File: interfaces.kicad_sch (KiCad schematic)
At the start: 125 parts, among them J3 USB-Micro-B_Amphenol_10118192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, J6 PinHeader_2x7_P2mm_Drill0.9mm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, J7 PinHeader_1x6_P2.54mm_Drill1.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, U1 MTFC16GAPALNA-AIT, U14 XC7A100T-FGG484, U17 USB3300-EZK-TR, U18 USB3300-EZK-TR, U19 FT4232H_QFN, U21 LSF0108RKSR, U22 LSF0101DRYR, U23 Oscillator_24MHz_ASEMB, U24 Oscillator_24MHz_ASEMB, U6 NVT2008BQ,115, Y1 Resonator_12MHz_ABM8G

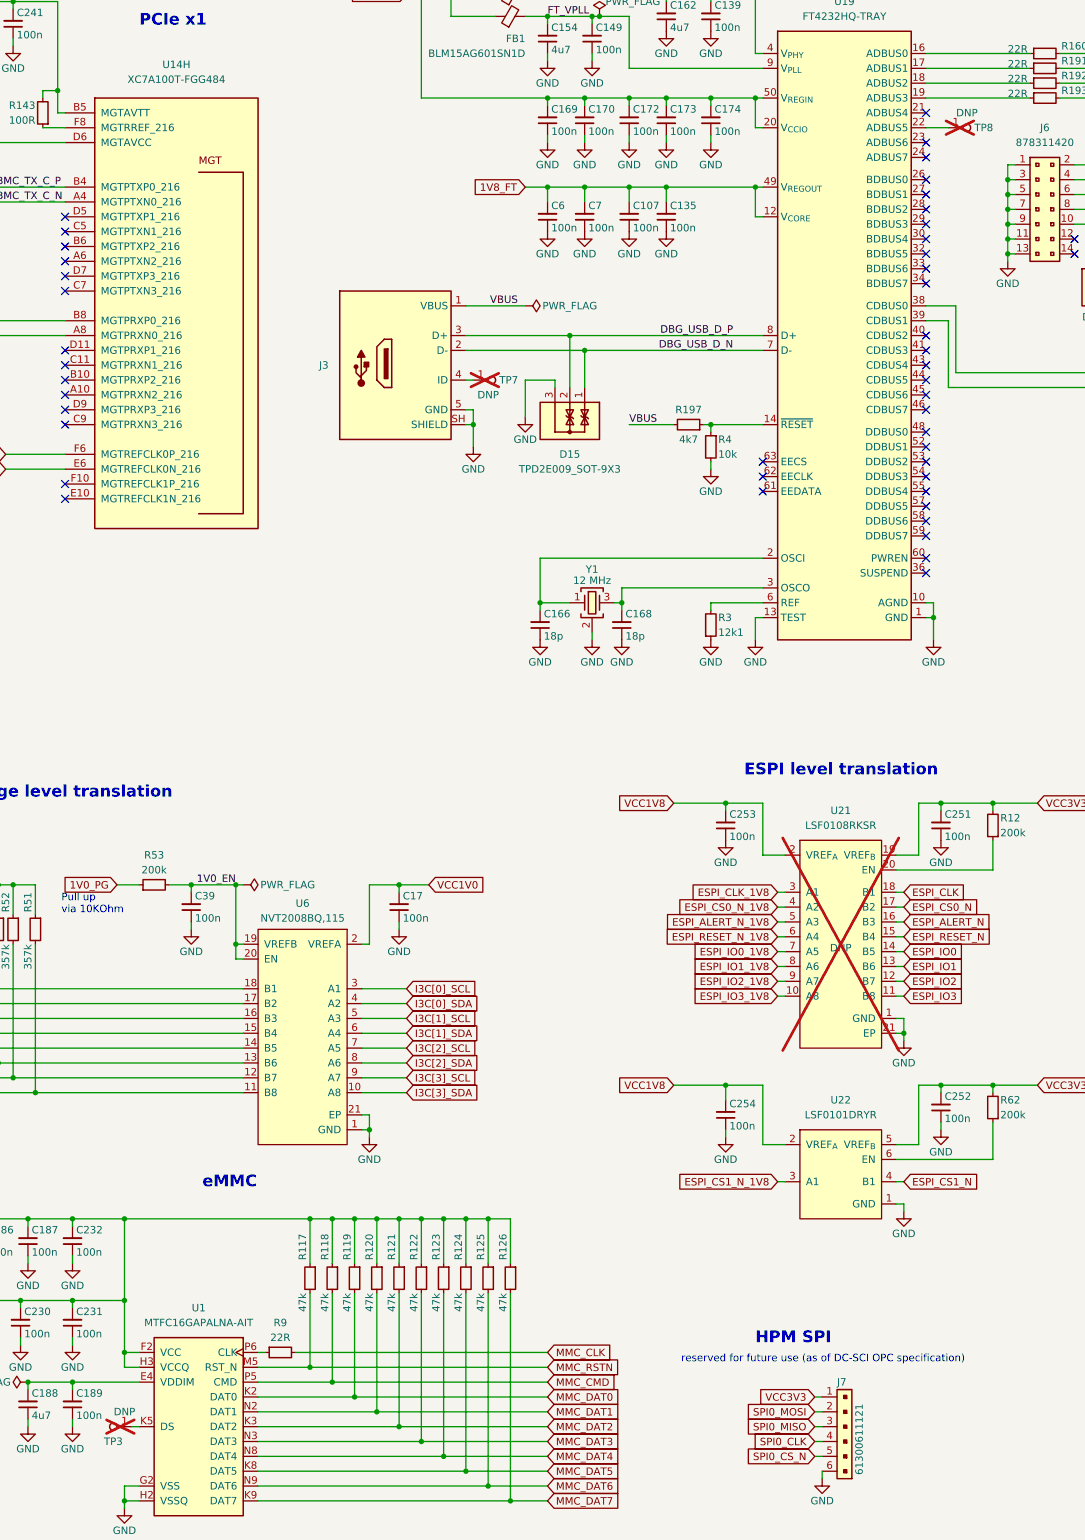
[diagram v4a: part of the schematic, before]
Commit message: [#68236] Remove DNP property from Testpoints
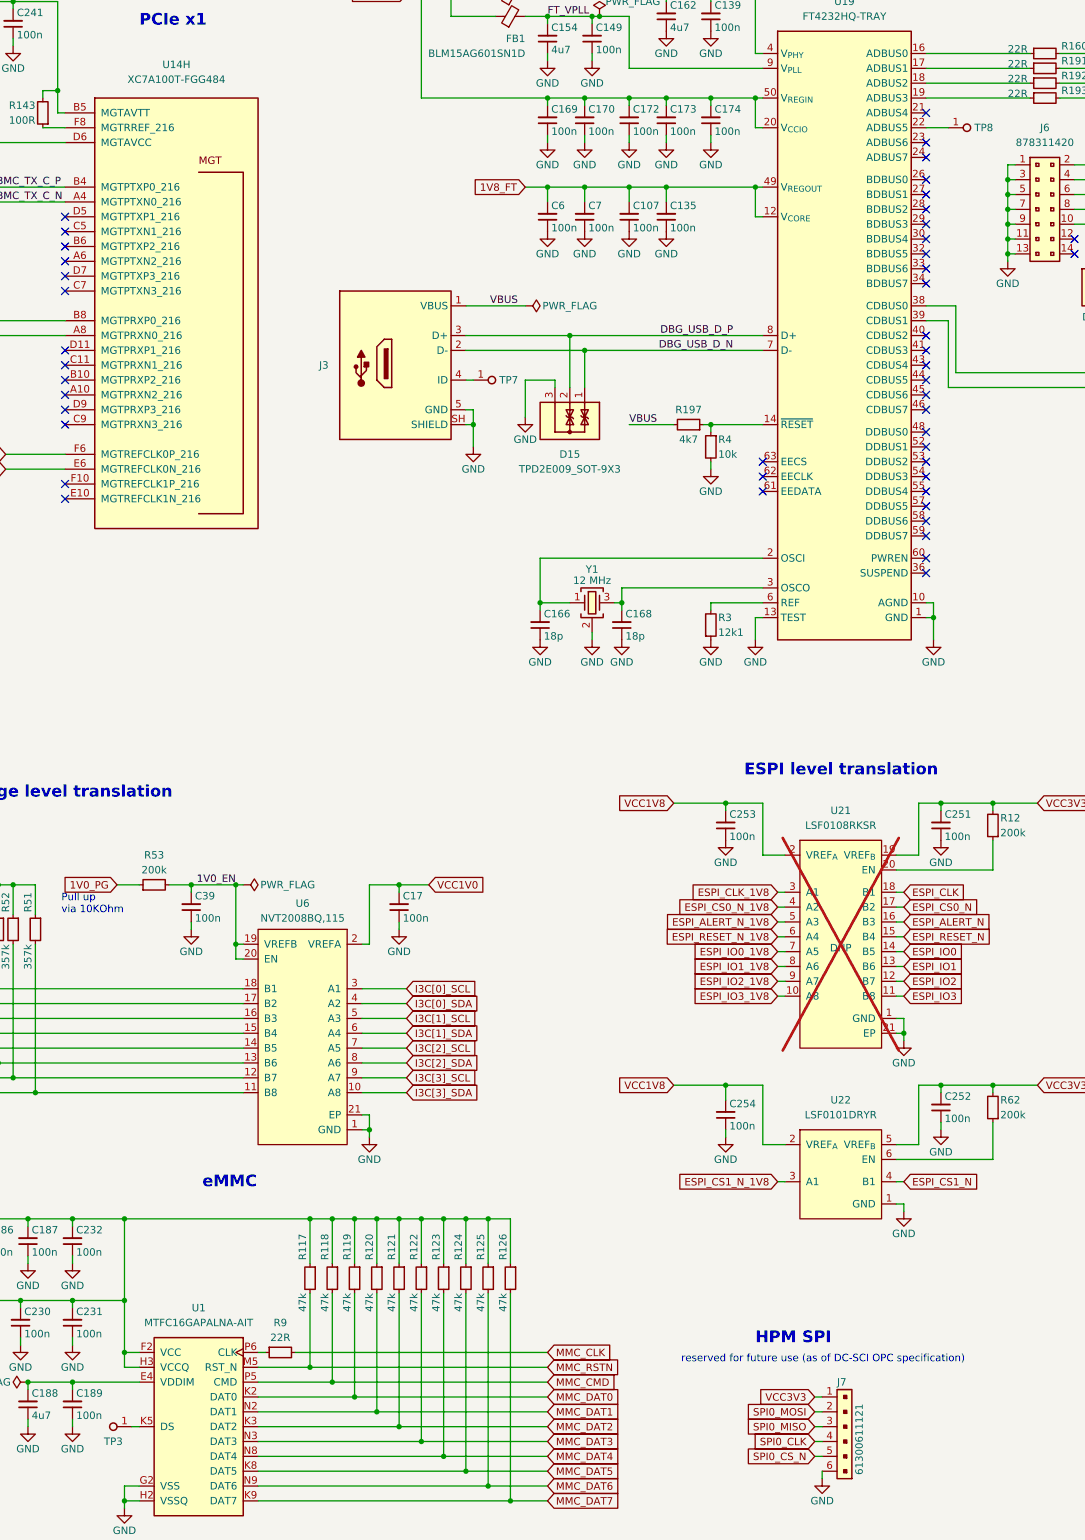
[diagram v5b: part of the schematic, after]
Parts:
- TP3, TP7, TP8: DNP DNP -> (none); now fitted
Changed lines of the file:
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@@
   )
   (symbol (lib_id "antmicroTestPoints:TP_1mm_SMD") (at 76.2 265.43 180) (unit 1)
-    (in_bom no) (on_board yes) (dnp yes)
+    (in_bom no) (on_board yes) (dnp no)
     (property "Reference" "TP3" (at 73.025 267.97 0)
       (effects (font (size 1.27 1.27)))
@@
       (effects (font (size 1.27 1.27) (thickness 0.15)) (justify left bottom) hide)
     )
-    (property "DNP" "DNP" (at 74.93 262.89 0)
-      (effects (font (size 1.27 1.27)))
-    )
     (pin "1")
     (instances
@@
   )
   (symbol (lib_id "antmicroTestPoints:TP_1mm_SMD") (at 134.62 86.36 0) (unit 1)
-    (in_bom no) (on_board yes) (dnp yes)
+    (in_bom no) (on_board yes) (dnp no)
     (property "Reference" "TP7" (at 139.065 86.36 0)
       (effects (font (size 1.27 1.27)) (justify left))
@@
       (effects (font (size 1.27 1.27) (thickness 0.15)) (justify left bottom) hide)
     )
-    (property "DNP" "DNP" (at 137.16 88.9 0)
-      (effects (font (size 1.27 1.27)))
-    )
     (pin "1")
     (instances
@@
   )
   (symbol (lib_id "antmicroTestPoints:TP_1mm_SMD") (at 215.9 43.18 0) (unit 1)
-    (in_bom no) (on_board yes) (dnp yes)
+    (in_bom no) (on_board yes) (dnp no)
     (property "Reference" "TP8" (at 220.345 43.18 0)
       (effects (font (size 1.27 1.27)) (justify left))
@@
       (effects (font (size 1.27 1.27) (thickness 0.15)) (justify left bottom) hide)
     )
-    (property "DNP" "DNP" (at 219.075 40.64 0)
-      (effects (font (size 1.27 1.27)))
-    )
     (pin "1")
